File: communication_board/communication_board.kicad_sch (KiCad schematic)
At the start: 0 parts

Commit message: Completed U1
added the MKR WAN 1310, and connected +5V, GND, and added Green, Yellow and Red lables
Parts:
- added U1: ~, symbol URC:MKR_WAN_1310_Arduino
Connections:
- new net +5V: U1.13 (VIN)
- new net GND: U1.11 (GND)
- new net Green: U1.6 (D11)
- new net Red: U1.9 (D14)
- new net Yellow: U1.8 (D13)

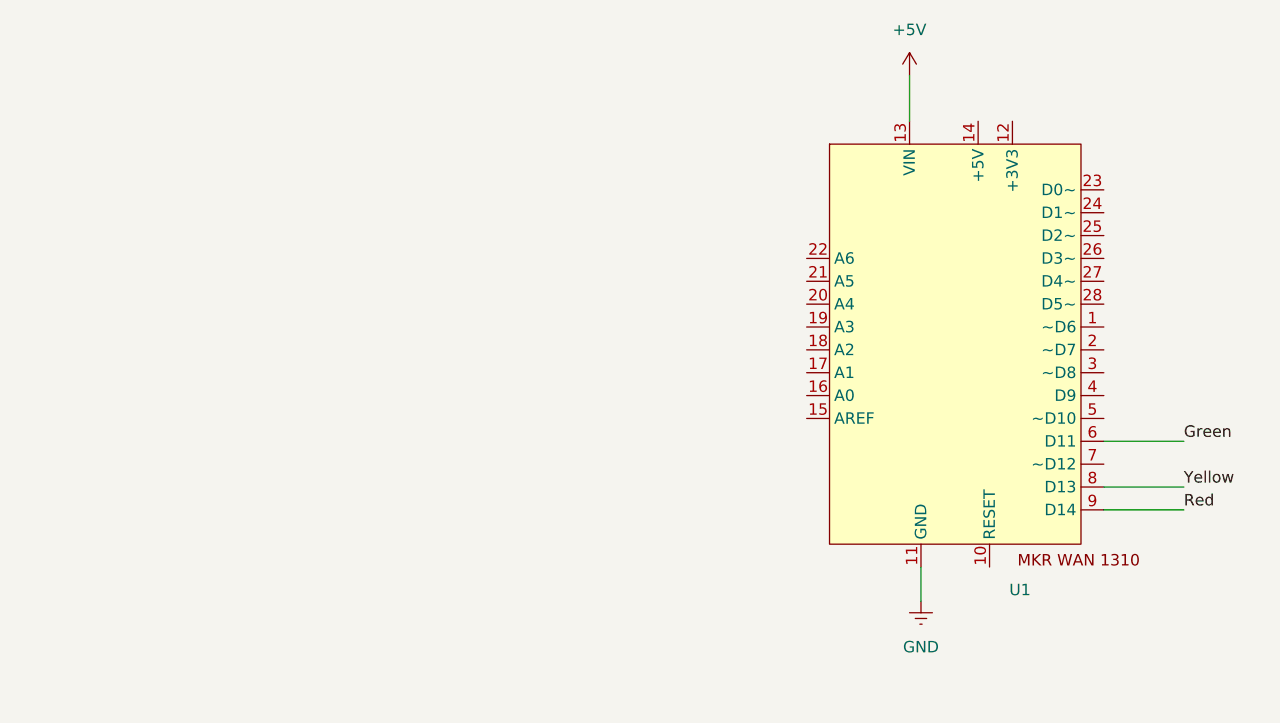
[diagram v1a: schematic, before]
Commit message: Added connector and resistor for red LED
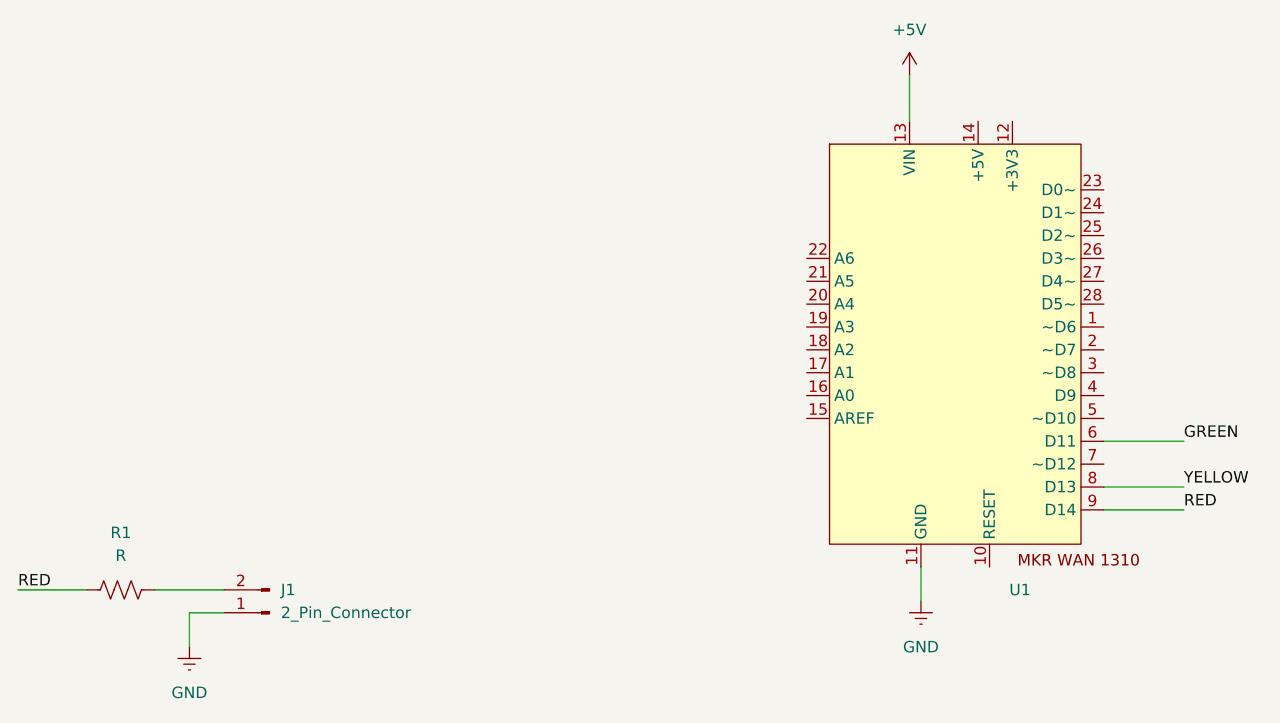
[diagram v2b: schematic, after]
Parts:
- added J1: 2_Pin_Connector, symbol URC:2_Pin_Connector
- added R1: R, symbol URC:R
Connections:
- net GND: now also J1.1 (Pin_1)
- net Green renamed GREEN
- net Red renamed RED
- net RED: now also R1.1
- net Yellow renamed YELLOW
- new net: J1.2 (Pin_2), R1.2

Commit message: added green
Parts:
- added J2, J3: 2_Pin_Connector, symbol URC:2_Pin_Connector
- added R2, R3: R, symbol URC:R
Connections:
- net GND: now also J2.1 (Pin_1), J3.1 (Pin_1)
- net GREEN: now also R3.1
- net YELLOW: now also R2.1
- new net: J2.2 (Pin_2), R2.2
- new net: J3.2 (Pin_2), R3.2
